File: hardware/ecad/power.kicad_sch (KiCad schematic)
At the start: 29 parts, among them J1 USB_C_Receptacle_USB2.0_14P, J2 Conn_01x02, U1 BQ24075RGT, U2 TPS62162DSG, U3 MT3608

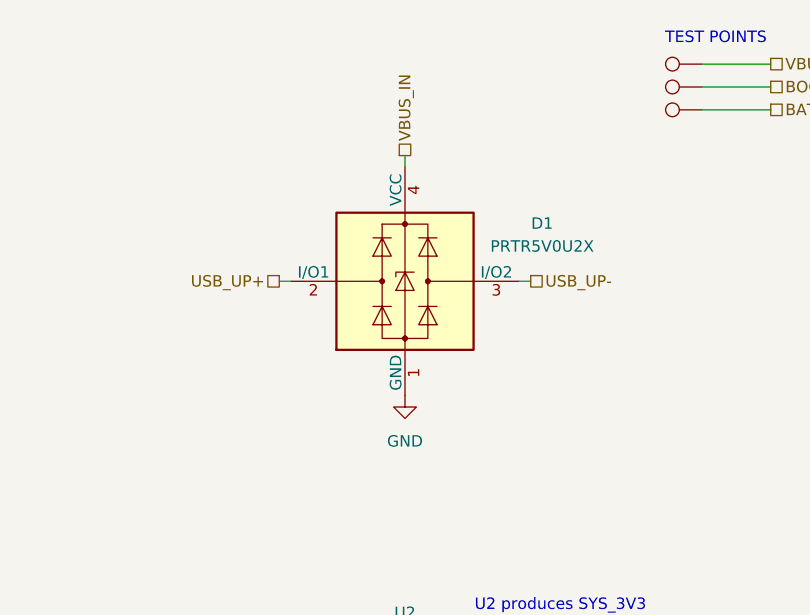
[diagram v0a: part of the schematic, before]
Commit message: Fixed minor errors and smaller issues withing schematics, moved v1 pcb and specific projet artifacts to archive. Updated changelog and finsihed pcb fopr version 2
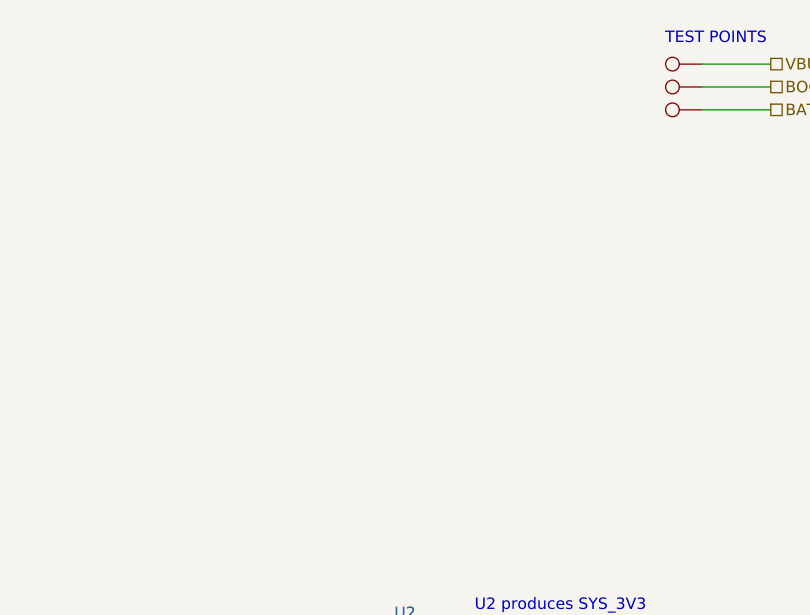
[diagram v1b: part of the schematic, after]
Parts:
- removed D1: PRTR5V0U2X, Package_TO_SOT_SMD:SOT-143, symbol Power_Protection:PRTR5V0U2X
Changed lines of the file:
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@@
 	(wire
 		(pts
-			(xy 154.94 41.91) (xy 156.21 41.91)
-		)
-		(stroke
-			(width 0)
-			(type default)
-		)
-	)
-	(wire
-		(pts
 			(xy 130.81 88.9) (xy 132.08 88.9)
 		)
@@
 	(wire
 		(pts
-			(xy 128.27 41.91) (xy 129.54 41.91)
-		)
-		(stroke
-			(width 0)
-			(type default)
-		)
-	)
-	(wire
-		(pts
 			(xy 16.51 116.84) (xy 40.64 116.84)
 		)
@@
 	(wire
 		(pts
-			(xy 142.24 29.21) (xy 142.24 27.94)
-		)
-		(stroke
-			(width 0)
-			(type default)
-		)
-	)
-	(wire
-		(pts
 			(xy 58.42 29.21) (xy 58.42 30.48)
 		)
@@
 		)
 	)
-	(hierarchical_label "VBUS_IN"
-		(shape passive)
-		(at 142.24 27.94 90)
-		(effects
-			(font
-				(size 1.27 1.27)
-			)
-			(justify left)
-		)
-	)
 	(hierarchical_label "BOOST_5V"
 		(shape passive)
@@
 		)
 	)
-	(hierarchical_label "USB_UP+"
-		(shape passive)
-		(at 128.27 41.91 180)
-		(effects
-			(font
-				(size 1.27 1.27)
-			)
-			(justify right)
-		)
-	)
-	(hierarchical_label "USB_UP-"
-		(shape passive)
-		(at 156.21 41.91 0)
-		(effects
-			(font
-				(size 1.27 1.27)
-			)
-			(justify left)
-		)
-	)
 	(hierarchical_label "BAT"
 		(shape passive)
@@
 	)
 	(symbol
-		(lib_id "Power_Protection:PRTR5V0U2X")
-		(at 142.24 41.91 0)
-		(unit 1)
-		(body_style 1)
-		(exclude_from_sim no)
-		(in_bom yes)
-		(on_board yes)
-		(in_pos_files yes)
-		(dnp no)
-		(fields_autoplaced yes)
-		(property "Reference" "D1"
-			(at 157.48 35.4898 0)
-			(show_name no)
-			(do_not_autoplace no)
-			(effects
-				(font
-					(size 1.27 1.27)
-				)
-			)
-		)
-		(property "Value" "PRTR5V0U2X"
-			(at 157.48 38.0298 0)
-			(show_name no)
-			(do_not_autoplace no)
-			(effects
-				(font
-					(size 1.27 1.27)
-				)
-			)
-		)
-		(property "Footprint" "Package_TO_SOT_SMD:SOT-143"
-			(at 143.764 41.91 0)
-			(hide yes)
-			(show_name no)
-			(do_not_autoplace no)
-			(effects
-				(font
-					(size 1.27 1.27)
-				)
-			)
-		)
-		(property "Datasheet" "https://assets.nexperia.com/documents/data-sheet/PRTR5V0U2X.pdf"
-			(at 143.764 41.91 0)
-			(hide yes)
-			(show_name no)
-			(do_not_autoplace no)
-			(effects
-				(font
-					(size 1.27 1.27)
-				)
-			)
-		)
-		(property "Description" "Ultra low capacitance double rail-to-rail ESD protection diode, SOT-143"
-			(at 142.24 41.91 0)
-			(hide yes)
-			(show_name no)
-			(do_not_autoplace no)
-			(effects
-				(font
-					(size 1.27 1.27)
-				)
-			)
-		)
-		(pin "2"
-		)
-		(pin "1"
-		)
-		(pin "3"
-		)
-		(pin "4"
-		)
-		(instances
-			(project "midi2BLE"
-				(path "/1637d879-66a9-4939-ab4a-2374b8e6eb1f/d6e8ba88-fb6c-44e1-88ab-cc4aae6bfb09"
-					(reference "D1")
-					(unit 1)
-				)
-			)
-		)
-	)
-	(symbol
 		(lib_id "Device:C")
 		(at 222.25 41.91 270)
@@
 					(unit 1)
 				)
-			)
-		)
-	)
-	(symbol
-		(lib_id "power:GND")
-		(at 142.24 54.61 0)
-		(unit 1)
-		(body_style 1)
-		(exclude_from_sim no)
-		(in_bom yes)
-		(on_board yes)
-		(in_pos_files yes)
-		(dnp no)
-		(fields_autoplaced yes)
-		(property "Reference" "#PWR03"
-			(at 142.24 60.96 0)
-			(hide yes)
-			(show_name no)
-			(do_not_autoplace no)
-			(effects
-				(font
-					(size 1.27 1.27)
-				)
-			)
-		)
-		(property "Value" "GND"
-			(at 142.24 59.69 0)
-			(show_name no)
-			(do_not_autoplace no)
-			(effects
-				(font
-					(size 1.27 1.27)
-				)
-			)
-		)
-		(property "Footprint" ""
-			(at 142.24 54.61 0)
-			(hide yes)
-			(show_name no)
-			(do_not_autoplace no)
-			(effects
-				(font
-					(size 1.27 1.27)
-				)
-			)
-		)
-		(property "Datasheet" ""
-			(at 142.24 54.61 0)
-			(hide yes)
-			(show_name no)
-			(do_not_autoplace no)
-			(effects
-				(font
-					(size 1.27 1.27)
-				)
-			)
-		)
-		(property "Description" "Power symbol creates a global label with name \"GND\" , ground"
-			(at 142.24 54.61 0)
-			(hide yes)
-			(show_name no)
-			(do_not_autoplace no)
-			(effects
-				(font
-					(size 1.27 1.27)
-				)
-			)
-		)
-		(pin "1"
-		)
-		(instances
-			(project "midi2BLE"
-				(path "/1637d879-66a9-4939-ab4a-2374b8e6eb1f/d6e8ba88-fb6c-44e1-88ab-cc4aae6bfb09"
-					(reference "#PWR03")
-					(unit 1)
-				)
